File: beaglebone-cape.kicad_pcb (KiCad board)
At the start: 2 copper layers, 86.4 x 54.6 mm, 56 parts, among them P1 BEAGLEBONE_BLACK, Q1 2N7000, Q2 2N7000, Q3 2N7000, Q4 2N7000, U2 V7805-2000, U3 4N25, U4 4N25

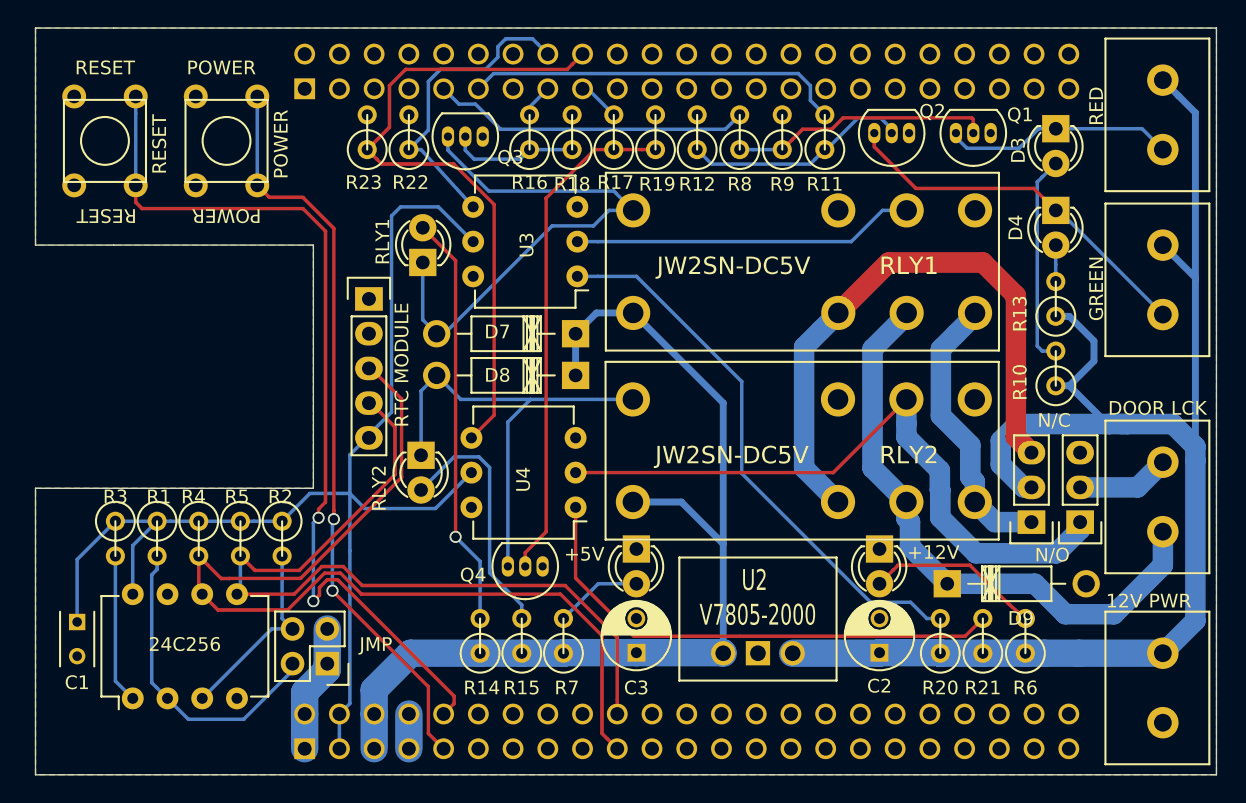
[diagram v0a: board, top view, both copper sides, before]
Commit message: Bumped up track width for 3.3V rail
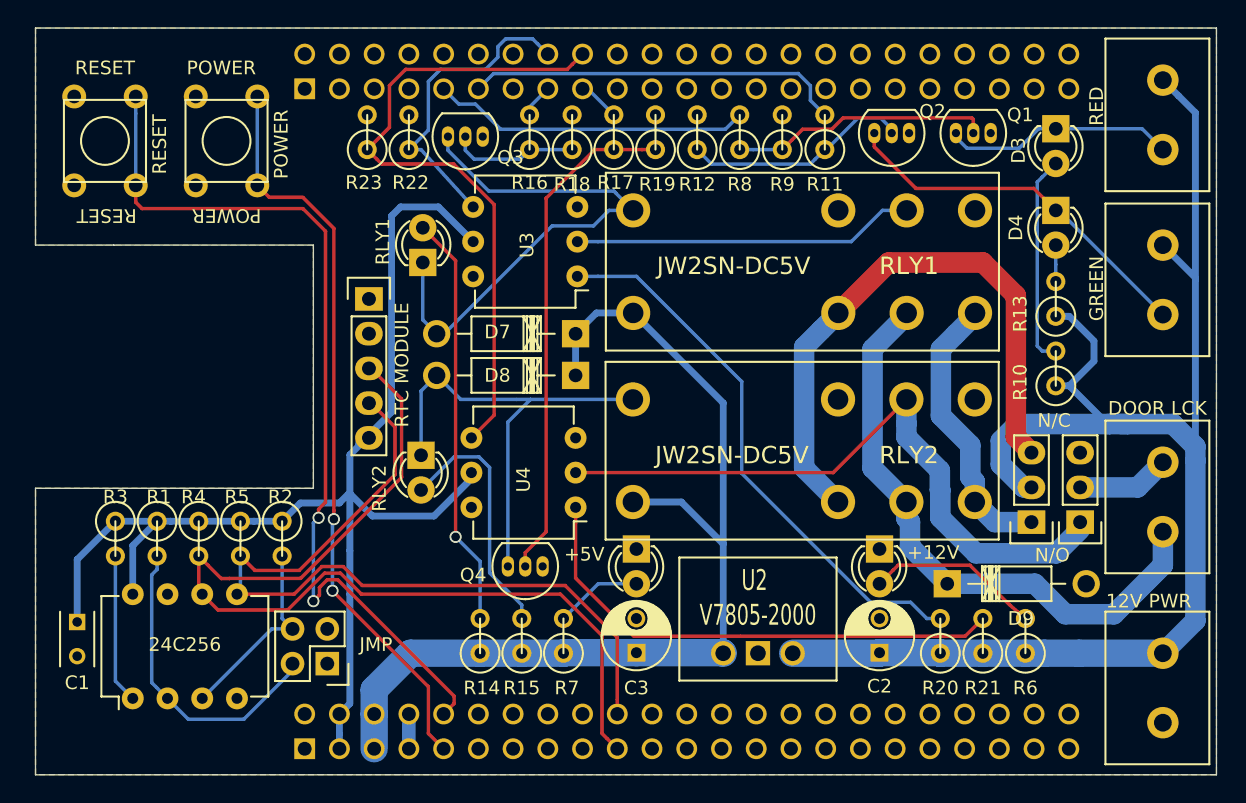
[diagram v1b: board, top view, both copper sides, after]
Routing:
- net GND: track 9.45 -> 0.00 mm
- net +3V3: track 91.7 -> 92.4 mm
- net Net-(P7-Pad1): track 48.6 -> 48.1 mm
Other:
- net class 3.3V Power added: clearance 0.2286, trace_width 0.5, via_dia 0.889, via_drill 0.635

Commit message: Added TODO list, almost there
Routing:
- net /SYS_RESETn: track 66.3 -> 65.1 mm
- net /I2C2_SDA: track 60.0 -> 59.0 mm
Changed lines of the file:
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@@
     (thickness 1.6)
     (drawings 15)
-    (tracks 360)
+    (tracks 357)
     (zones 0)
     (modules 56)
@@
   (segment (start 113.284 129.032) (end 111.76 129.032) (width 0.254) (layer B.Cu) (net 3))
   (segment (start 111.76 129.032) (end 106.68 134.112) (width 0.254) (layer B.Cu) (net 3))
-  (segment (start 121.259611 112.217211) (end 121.259611 117.951694) (width 0.254) (layer F.Cu) (net 4))
+  (segment (start 108.65271 125.349) (end 108.077 125.349) (width 0.254) (layer F.Cu) (net 4))
+  (segment (start 108.665311 125.336399) (end 108.65271 125.349) (width 0.254) (layer F.Cu) (net 4))
+  (segment (start 118.872 109.982) (end 119.0244 109.982) (width 0.254) (layer F.Cu) (net 4))
   (segment (start 119.0244 109.982) (end 121.259611 112.217211) (width 0.254) (layer F.Cu) (net 4))
+  (segment (start 121.259611 112.217211) (end 121.259611 117.690889) (width 0.254) (layer F.Cu) (net 4))
+  (segment (start 121.259611 117.690889) (end 113.614101 125.336399) (width 0.254) (layer F.Cu) (net 4))
+  (segment (start 113.614101 125.336399) (end 108.665311 125.336399) (width 0.254) (layer F.Cu) (net 4))
+  (segment (start 108.077 125.349) (end 107.124499 124.396499) (width 0.254) (layer F.Cu) (net 4))
+  (segment (start 107.124499 124.396499) (end 106.426 123.698) (width 0.254) (layer F.Cu) (net 4))
   (segment (start 135.915399 129.529329) (end 135.915399 136.677399) (width 0.254) (layer F.Cu) (net 4))
-  (segment (start 108.077 125.349) (end 107.124499 124.396499) (width 0.254) (layer F.Cu) (net 4))
-  (segment (start 118.872 109.982) (end 119.0244 109.982) (width 0.254) (layer F.Cu) (net 4))
   (segment (start 115.621046 124.955287) (end 116.788954 124.955287) (width 0.254) (layer F.Cu) (net 4))
   (segment (start 118.325667 126.492) (end 132.87807 126.492) (width 0.254) (layer F.Cu) (net 4))
   (segment (start 106.68 126.492) (end 107.835601 127.647601) (width 0.254) (layer F.Cu) (net 4))
-  (segment (start 113.874906 125.336399) (end 108.665311 125.336399) (width 0.254) (layer F.Cu) (net 4))
   (segment (start 112.928732 127.647601) (end 115.621046 124.955287) (width 0.254) (layer F.Cu) (net 4))
-  (segment (start 107.124499 124.396499) (end 106.426 123.698) (width 0.254) (layer F.Cu) (net 4))
-  (segment (start 108.665311 125.336399) (end 108.65271 125.349) (width 0.254) (layer F.Cu) (net 4))
-  (segment (start 108.65271 125.349) (end 108.077 125.349) (width 0.254) (layer F.Cu) (net 4))
   (segment (start 116.788954 124.955287) (end 118.325667 126.492) (width 0.254) (layer F.Cu) (net 4))
   (segment (start 107.835601 127.647601) (end 112.928732 127.647601) (width 0.254) (layer F.Cu) (net 4))
   (segment (start 132.87807 126.492) (end 135.915399 129.529329) (width 0.254) (layer F.Cu) (net 4))
-  (segment (start 121.259611 117.951694) (end 113.874906 125.336399) (width 0.254) (layer F.Cu) (net 4))
   (segment (start 135.915399 136.677399) (end 136.271001 137.033001) (width 0.254) (layer F.Cu) (net 4))
   (segment (start 136.271001 137.033001) (end 137.033 137.795) (width 0.254) (layer F.Cu) (net 4))
@@
   (segment (start 106.426 126.238) (end 106.68 126.492) (width 0.254) (layer F.Cu) (net 4))
   (segment (start 119.0244 112.522) (end 118.872 112.522) (width 0.254) (layer F.Cu) (net 5))
-  (segment (start 113.776689 124.752101) (end 120.777 117.75179) (width 0.254) (layer F.Cu) (net 5))
+  (segment (start 110.528101 122.643899) (end 115.624087 122.643899) (width 0.254) (layer F.Cu) (net 5))
+  (segment (start 120.777 117.490986) (end 120.777 114.2746) (width 0.254) (layer F.Cu) (net 5))
+  (segment (start 109.474 123.698) (end 110.528101 122.643899) (width 0.254) (layer F.Cu) (net 5))
+  (segment (start 120.777 114.2746) (end 119.0244 112.522) (width 0.254) (layer F.Cu) (net 5))
+  (segment (start 115.624087 122.643899) (end 120.777 117.490986) (width 0.254) (layer F.Cu) (net 5))
   (segment (start 118.373182 125.857) (end 133.223 125.857) (width 0.254) (layer F.Cu) (net 5))
   (segment (start 137.033 129.667) (end 137.033 134.17737) (width 0.254) (layer F.Cu) (net 5))
   (segment (start 137.033 134.17737) (end 137.033 135.255) (width 0.254) (layer F.Cu) (net 5))
-  (segment (start 120.777 114.2746) (end 119.0244 112.522) (width 0.254) (layer F.Cu) (net 5))
   (segment (start 109.22 126.492) (end 113.401818 126.492) (width 0.254) (layer F.Cu) (net 5))
   (segment (start 116.988858 124.472676) (end 118.373182 125.857) (width 0.254) (layer F.Cu) (net 5))
-  (segment (start 109.474 123.698) (end 110.528101 124.752101) (width 0.254) (layer F.Cu) (net 5))
   (segment (start 113.401818 126.492) (end 115.421142 124.472676) (width 0.254) (layer F.Cu) (net 5))
-  (segment (start 110.528101 124.752101) (end 113.776689 124.752101) (width 0.254) (layer F.Cu) (net 5))
   (segment (start 133.223 125.857) (end 137.033 129.667) (width 0.254) (layer F.Cu) (net 5))
   (segment (start 115.421142 124.472676) (end 116.988858 124.472676) (width 0.254) (layer F.Cu) (net 5))
-  (segment (start 120.777 117.75179) (end 120.777 114.2746) (width 0.254) (layer F.Cu) (net 5))
   (segment (start 109.474 126.238) (end 109.22 126.492) (width 0.254) (layer B.Cu) (net 5))
   (segment (start 109.474 123.698) (end 109.474 126.238) (width 0.254) (layer B.Cu) (net 5))
@@
   (segment (start 120.370601 89.303349) (end 121.561349 88.112601) (width 0.254) (layer F.Cu) (net 37))
   (segment (start 121.561349 88.112601) (end 133.375399 88.112601) (width 0.254) (layer F.Cu) (net 37))
-  (segment (start 110.708 96.595) (end 111.582999 97.469999) (width 0.254) (layer F.Cu) (net 66))
-  (segment (start 111.582999 97.469999) (end 114.037999 97.469999) (width 0.254) (layer F.Cu) (net 66))
-  (segment (start 114.037999 97.469999) (end 116.306348 99.738348) (width 0.254) (layer F.Cu) (net 66))
+  (segment (start 116.205 126.238) (end 116.205 120.931446) (width 0.254) (layer B.Cu) (net 66))
+  (segment (start 116.218028 120.289801) (end 116.218028 120.918418) (width 0.254) (layer F.Cu) (net 66))
+  (segment (start 113.163 96.595) (end 116.218028 99.650028) (width 0.254) (layer F.Cu) (net 66))
+  (segment (start 116.205 120.931446) (end 116.218028 120.918418) (width 0.254) (layer B.Cu) (net 66))
+  (segment (start 116.218028 99.650028) (end 116.218028 120.289801) (width 0.254) (layer F.Cu) (net 66))
+  (segment (start 110.708 96.595) (end 113.163 96.595) (width 0.254) (layer F.Cu) (net 66))
+  (via (at 116.218028 120.918418) (size 0.889) (drill 0.635) (layers F.Cu B.Cu) (net 66))
   (segment (start 110.708 90.095) (end 110.708 96.595) (width 0.254) (layer B.Cu) (net 66))
-  (via (at 116.306348 121.006737) (size 0.889) (drill 0.635) (layers F.Cu B.Cu) (net 66))
-  (segment (start 116.306348 99.738348) (end 116.306348 120.37812) (width 0.254) (layer F.Cu) (net 66))
-  (segment (start 116.306348 120.37812) (end 116.306348 121.006737) (width 0.254) (layer F.Cu) (net 66))
-  (segment (start 116.205 126.238) (end 116.205 121.108085) (width 0.254) (layer B.Cu) (net 66))
-  (segment (start 116.205 121.108085) (end 116.306348 121.006737) (width 0.254) (layer B.Cu) (net 66))
   (segment (start 123.215399 136.677399) (end 123.215399 133.248399) (width 0.254) (layer F.Cu) (net 66))
   (segment (start 124.333 137.795) (end 123.215399 136.677399) (width 0.254) (layer F.Cu) (net 66))
   (segment (start 123.215399 133.248399) (end 116.205 126.238) (width 0.254) (layer F.Cu) (net 66))
   (via (at 116.205 126.238) (size 0.889) (drill 0.635) (layers F.Cu B.Cu) (net 66))
-  (segment (start 102.283564 98.298) (end 114.046 98.298) (width 0.254) (layer F.Cu) (net 67))
-  (segment (start 114.046 98.298) (end 115.697 99.949) (width 0.254) (layer F.Cu) (net 67))
-  (segment (start 101.818 96.595) (end 101.818 97.832436) (width 0.254) (layer F.Cu) (net 67))
-  (segment (start 101.818 97.832436) (end 102.283564 98.298) (width 0.254) (layer F.Cu) (net 67))
+  (segment (start 115.10055 99.35255) (end 115.10055 120.272449) (width 0.254) (layer F.Cu) (net 67))
+  (segment (start 101.818 96.595) (end 103.521 98.298) (width 0.254) (layer F.Cu) (net 67))
+  (segment (start 103.521 98.298) (end 114.046 98.298) (width 0.254) (layer F.Cu) (net 67))
+  (segment (start 114.808 127) (end 114.808 121.193616) (width 0.254) (layer B.Cu) (net 67))
+  (segment (start 114.808 121.193616) (end 115.10055 120.901066) (width 0.254) (layer B.Cu) (net 67))
+  (segment (start 114.046 98.298) (end 115.10055 99.35255) (width 0.254) (layer F.Cu) (net 67))
+  (via (at 115.10055 120.901066) (size 0.889) (drill 0.635) (layers F.Cu B.Cu) (net 67))
+  (segment (start 115.10055 120.272449) (end 115.10055 120.901066) (width 0.254) (layer F.Cu) (net 67))
   (segment (start 101.818 90.095) (end 101.818 91.332436) (width 0.254) (layer B.Cu) (net 67))
   (segment (start 101.818 91.332436) (end 101.818 96.595) (width 0.254) (layer B.Cu) (net 67))
-  (segment (start 115.697 119.767383) (end 115.697 99.949) (width 0.254) (layer F.Cu) (net 67))
-  (segment (start 115.189 120.904) (end 115.189 120.275383) (width 0.254) (layer F.Cu) (net 67))
-  (segment (start 115.189 120.275383) (end 115.697 119.767383) (width 0.254) (layer F.Cu) (net 67))
-  (segment (start 114.808 127) (end 114.808 121.285) (width 0.254) (layer B.Cu) (net 67))
-  (via (at 115.189 120.904) (size 0.889) (drill 0.635) (layers F.Cu B.Cu) (net 67))
-  (segment (start 114.808 121.285) (end 115.189 120.904) (width 0.254) (layer B.Cu) (net 67))
   (segment (start 124.333 135.255) (end 125.094999 134.493001) (width 0.254) (layer F.Cu) (net 67))
   (segment (start 115.82095 125.437898) (end 115.252499 126.006349) (width 0.254) (layer F.Cu) (net 67))

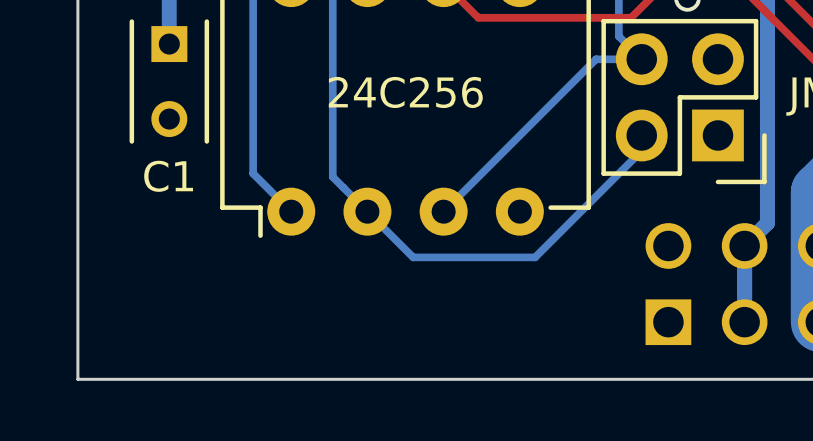
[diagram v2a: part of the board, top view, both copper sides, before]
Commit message: Added silkscreen comments, copyright
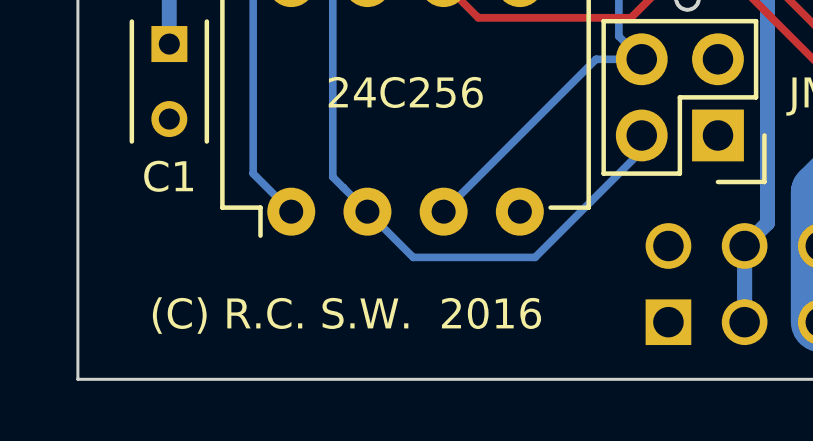
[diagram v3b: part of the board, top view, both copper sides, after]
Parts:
- added REF**: Symbol_GNU-Logo_SilkscreenTop, Symbols:Symbol_GNU-Logo_SilkscreenTop, B.Cu at (145.4, 102.9)
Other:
- board text added: "(C) R.C. S.W. 2016"
- board text added: "(C) R.C., S.W. 2016"
- board text added: "V3"

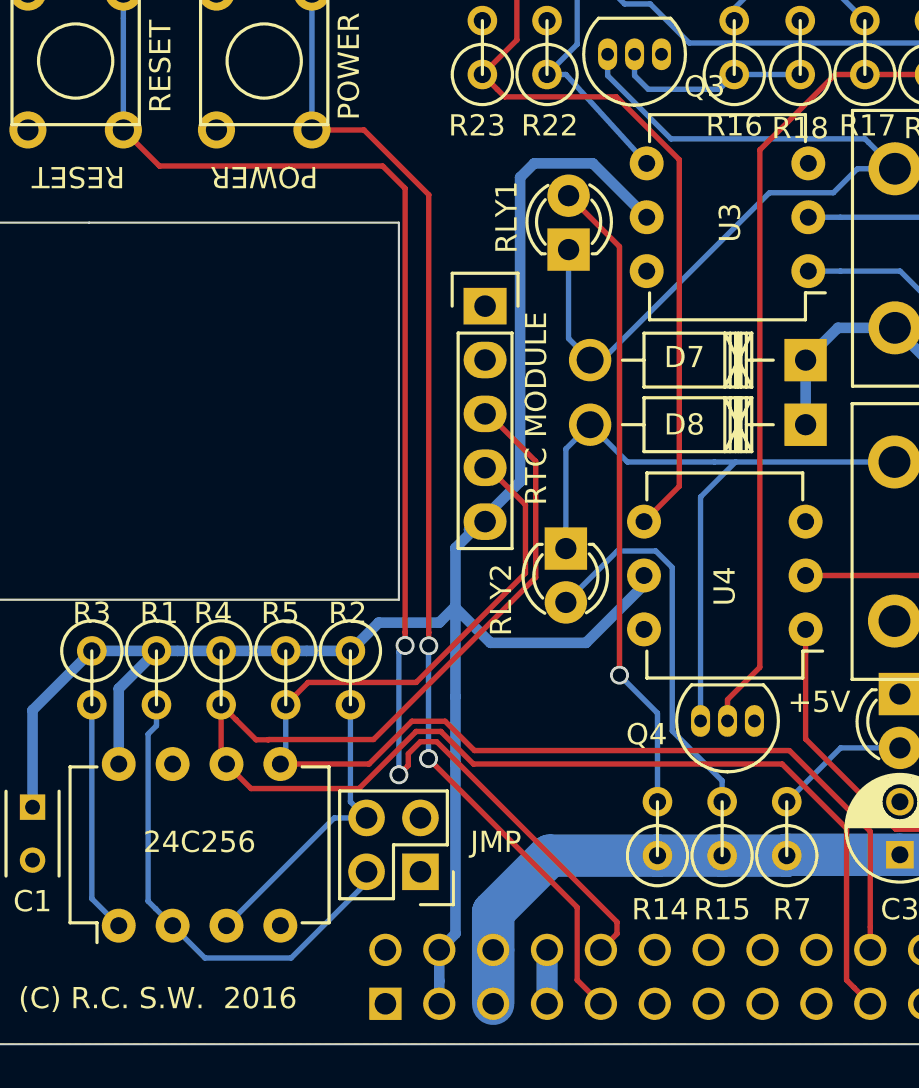
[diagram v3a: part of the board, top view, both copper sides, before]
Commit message: Flipped RTC module, rearranged resistors R1-R5, add A0 A1 to silk screen for jumpers
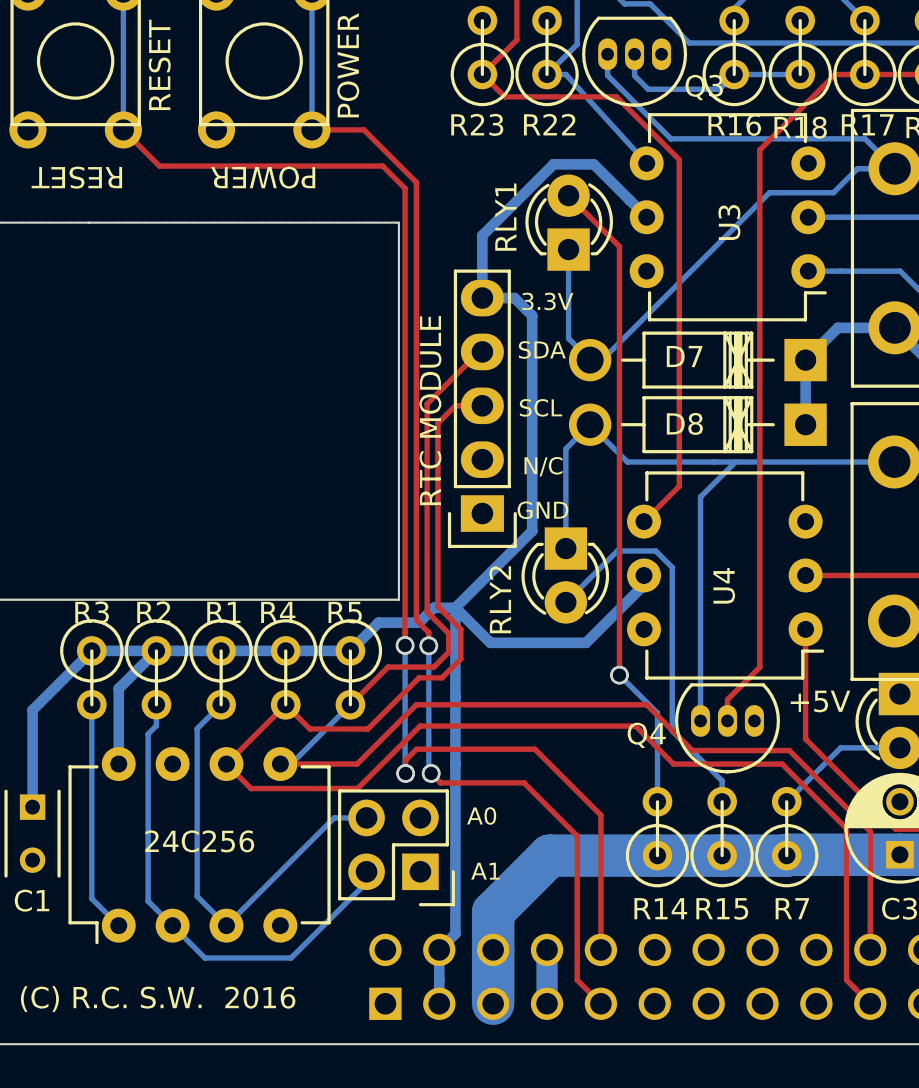
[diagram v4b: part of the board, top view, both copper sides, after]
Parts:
- moved RTC MODULE 9.78 mm to (118.7, 114.7), turned to 180 degrees
- moved R2 9.14 mm to (103.4, 122.4)
- moved R1 3.05 mm to (106.4, 122.4)
- moved R4 3.05 mm to (109.5, 122.4)
- moved R5 3.05 mm to (112.5, 122.4)
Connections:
- R1 pad 2: /A1 -> /A2
- R2 pad 2: /A2 -> /A1
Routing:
- net /A2: track 14.4 -> 20.2 mm
- net /I2C2_SDA: track 59.0 -> 63.3 mm
- net /PWR_BUT: track 54.8 -> 57.1 mm
- net /I2C2_SCL: track 72.0 -> 70.2 mm
- net +3V3: track 92.4 -> 93.8 mm
- net /SYS_RESETn: track 65.1 -> 66.2 mm
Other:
- board text added: "3.3V"
- board text added: "A0"
- board text added: "A1"
- board text added: "GND"
- board text added: "SCL"
- board text added: "SDA"
